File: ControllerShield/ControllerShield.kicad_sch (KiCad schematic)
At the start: 17 parts, among them J1 Power, J2 Digital/PWM, J3 Analog, J4 Digital/PWM, J5 Conn_02x05_Odd_Even, U1 COM-09032, U2 LIS3DH, U3 TLV75533PDBV

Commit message: Add switch to controller
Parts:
- added SW1: Small Switch TH, Footprints:SW4_1825910-B_TEC, symbol Local:Small Switch TH
- C1: Digikey (none) -> 1276-1000-1-ND
- C2: Digikey (none) -> 490-GRM188R61E106KA73JCT-ND
- D1: Digikey (none) -> 1125-1188-ND
- D2: Digikey (none) -> 1125-1184-ND
- R1, R2: Digikey (none) -> RMCF0603FT10K0CT-ND
- R3, R4: Digikey (none) -> RMCF0603FT1K00CT-ND
- U2: value LIS3DH -> LIS2DE12TR; Digikey (none) -> 497-15997-1-ND
- U3: Digikey (none) -> 296-50411-1-ND
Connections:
- net GND: now also SW1.3 (B), SW1.4 (B)
- net ~{RESET} renamed RSTn
- net RSTn: now also SW1.1 (A), SW1.2 (A)
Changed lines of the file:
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@@
+    (stroke (width 0) (type default))
+  )
+  (wire (pts (xy 54.61 138.43) (xy 63.5 138.43))
     (stroke (width 0) (type default))
   )
@@
     (effects (font (size 1.27 1.27)) (justify left bottom))
   )
-  (label "~{RESET}" (at 19.05 36.83 0) (fields_autoplaced)
-    (effects (font (size 1.27 1.27)) (justify left bottom))
+  (label "RSTn" (at 19.05 36.83 180) (fields_autoplaced)
+    (effects (font (size 1.27 1.27)) (justify right bottom))
   )
   (label "GameBtn" (at 68.58 72.39 0) (fields_autoplaced)
@@
   (label "X" (at 72.39 46.99 180) (fields_autoplaced)
     (effects (font (size 1.27 1.27)) (justify right bottom))
+  )
+  (label "RSTn" (at 55.88 138.43 0) (fields_autoplaced)
+    (effects (font (size 1.27 1.27)) (justify left bottom))
   )
   (label "D1" (at 69.85 39.37 0) (fields_autoplaced)
@@
     )
     (property "Datasheet" "~" (at 133.35 113.03 0)
+      (effects (font (size 1.27 1.27)) hide)
+    )
+    (property "Digikey" "RMCF0603FT10K0CT-ND" (at 133.35 113.03 0)
       (effects (font (size 1.27 1.27)) hide)
     )
@@
       (effects (font (size 1.27 1.27)) hide)
     )
+    (property "Digikey" "RMCF0603FT1K00CT-ND" (at 116.84 45.72 0)
+      (effects (font (size 1.27 1.27)) hide)
+    )
     (pin "1")
     (pin "2")
@@
         (path "/e63e39d7-6ac0-4ffd-8aa3-1841a4541b55"
           (reference "R4") (unit 1)
+        )
+      )
+    )
+  )
+  (symbol (lib_id "power:GND") (at 73.66 138.43 0) (unit 1)
+    (in_bom yes) (on_board yes) (dnp no) (fields_autoplaced)
+    (property "Reference" "#PWR011" (at 73.66 144.78 0)
+      (effects (font (size 1.27 1.27)) hide)
+    )
+    (property "Value" "GND" (at 73.66 143.51 0)
+      (effects (font (size 1.27 1.27)))
+    )
+    (property "Footprint" "" (at 73.66 138.43 0)
+      (effects (font (size 1.27 1.27)) hide)
+    )
+    (property "Datasheet" "" (at 73.66 138.43 0)
+      (effects (font (size 1.27 1.27)) hide)
+    )
+    (pin "1")
+    (instances
+      (project "ControllerShield"
+        (path "/e63e39d7-6ac0-4ffd-8aa3-1841a4541b55"
+          (reference "#PWR011") (unit 1)
         )
       )
@@
       (effects (font (size 1.27 1.27)) hide)
     )
-    (property "Datasheet" "~" (at 116.84 54.61 0)
+    (property "Datasheet" "https://marktechopto.com/pdf/products/datasheet/MT2118-G-A.pdf" (at 116.84 54.61 0)
+      (effects (font (size 1.27 1.27)) hide)
+    )
+    (property "Digikey" "1125-1184-ND" (at 116.84 54.61 0)
       (effects (font (size 1.27 1.27)) hide)
     )
@@
     )
     (property "Datasheet" "http://www.ti.com/lit/ds/symlink/tlv755p.pdf" (at 127 77.47 0)
+      (effects (font (size 1.27 1.27)) hide)
+    )
+    (property "Digikey" "296-50411-1-ND" (at 127 78.74 0)
       (effects (font (size 1.27 1.27)) hide)
     )
@@
       (effects (font (size 1.27 1.27)) hide)
     )
+    (property "Digikey" "RMCF0603FT10K0CT-ND" (at 130.81 113.03 0)
+      (effects (font (size 1.27 1.27)) hide)
+    )
     (pin "1")
     (pin "2")
@@
       (effects (font (size 1.27 1.27)) (justify left))
     )
-    (property "Value" "LIS3DH" (at 161.29 132.08 0)
+    (property "Value" "LIS2DE12TR" (at 161.29 132.08 0)
       (effects (font (size 1.27 1.27)) (justify left))
     )
@@
       (effects (font (size 1.27 1.27)) hide)
     )
-    (property "Datasheet" "https://www.st.com/resource/en/datasheet/cd00274221.pdf" (at 153.67 124.46 0)
+    (property "Datasheet" "https://www.st.com/content/ccc/resource/technical/document/datasheet/group0/72/cb/80/a7/5e/fe/46/9d/DM00153214/files/DM00153214.pdf/jcr:content/translations/en.DM00153214.pdf" (at 153.67 124.46 0)
+      (effects (font (size 1.27 1.27)) hide)
+    )
+    (property "Digikey" "497-15997-1-ND" (at 158.75 121.92 0)
       (effects (font (size 1.27 1.27)) hide)
     )
@@
       (effects (font (size 1.27 1.27)) hide)
     )
+    (property "Digikey" "1125-1188-ND" (at 109.22 54.61 0)
+      (effects (font (size 1.27 1.27)) hide)
+    )
     (pin "1")
     (pin "2")
@@
       (effects (font (size 1.27 1.27)) hide)
     )
+    (property "Digikey" "490-GRM188R61E106KA73JCT-ND" (at 191.77 118.11 0)
+      (effects (font (size 1.27 1.27)) hide)
+    )
     (pin "1")
     (pin "2")
@@
     )
   )
+  (symbol (lib_id "Local:Small Switch TH") (at 68.58 138.43 0) (unit 1)
+    (in_bom yes) (on_board yes) (dnp no) (fields_autoplaced)
+    (property "Reference" "SW1" (at 68.58 132.08 0)
+      (effects (font (size 1.27 1.27)))
+    )
+    (property "Value" "Small Switch TH" (at 68.58 134.62 0)
+      (effects (font (size 1.27 1.27)))
+    )
+    (property "Footprint" "Footprints:SW4_1825910-B_TEC" (at 68.58 138.43 0)
+      (effects (font (size 1.27 1.27)) hide)
+    )
+    (property "Datasheet" "https://www.te.com/usa-en/product-1825910-6.datasheet.pdf" (at 68.58 138.43 0)
+      (effects (font (size 1.27 1.27)) hide)
+    )
+    (property "Digikey" "450-1650-ND" (at 68.58 138.43 0)
+      (effects (font (size 1.27 1.27)) hide)
+    )
+    (pin "1")
+    (pin "2")
+    (pin "3")
+    (pin "4")
+    (instances
+      (project "ControllerShield"
+        (path "/e63e39d7-6ac0-4ffd-8aa3-1841a4541b55"
+          (reference "SW1") (unit 1)
+        )
+      )
+    )
+  )
   (symbol (lib_id "power:+3V3") (at 156.21 109.22 0) (unit 1)
     (in_bom yes) (on_board yes) (dnp no)
@@
       (effects (font (size 1.27 1.27)) hide)
     )
+    (property "Digikey" "1276-1000-1-ND" (at 180.34 118.11 0)
+      (effects (font (size 1.27 1.27)) hide)
+    )
     (pin "1")
     (pin "2")
@@
       (effects (font (size 1.27 1.27)) hide)
     )
+    (property "Digikey" "RMCF0603FT1K00CT-ND" (at 109.22 45.72 0)
+      (effects (font (size 1.27 1.27)) hide)
+    )

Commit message: add probe points
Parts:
- added J6: Debug Point, Connector_PinHeader_2.54mm:PinHeader_1x03_P2.54mm_Vertical, symbol Connector_Generic:Conn_01x03
- U2: value LIS2DE12TR -> LIS3DHTR; Digikey 497-15997-1-ND -> 497-10613-1-ND
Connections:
- net GND: now also J6.2 (Pin_2)
- net X: now also J6.1 (Pin_1)
- net Y: now also J6.3 (Pin_3)
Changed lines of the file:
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@@
     (date "2023-10-11")
   )
+  (junction (at 99.06 101.6) (diameter 0) (color 0 0 0 0)
+  )
   (junction (at 173.99 39.37) (diameter 0) (color 0 0 0 0)
+  )
+  (junction (at 81.28 101.6) (diameter 0) (color 0 0 0 0)
   )
   (junction (at 130.81 107.95) (diameter 0) (color 0 0 0 0)
@@
     (stroke (width 0) (type solid))
   )
+  (wire (pts (xy 88.9 91.44) (xy 88.9 93.98))
+    (stroke (width 0) (type default))
+  )
+  (wire (pts (xy 93.98 91.44) (xy 93.98 93.98))
+    (stroke (width 0) (type default))
+  )
   (wire (pts (xy 62.23 44.45) (xy 74.93 44.45))
     (stroke (width 0) (type solid))
@@
     (stroke (width 0) (type default))
   )
-  (wire (pts (xy 85.09 101.6) (xy 71.12 101.6))
+  (wire (pts (xy 85.09 101.6) (xy 81.28 101.6))
     (stroke (width 0) (type default))
   )
@@
     (stroke (width 0) (type default))
   )
+  (wire (pts (xy 93.98 93.98) (xy 99.06 93.98))
+    (stroke (width 0) (type default))
+  )
   (wire (pts (xy 177.8 72.39) (xy 177.8 77.47))
     (stroke (width 0) (type default))
@@
     (stroke (width 0) (type default))
   )
-  (wire (pts (xy 97.79 101.6) (xy 106.68 101.6))
+  (wire (pts (xy 97.79 101.6) (xy 99.06 101.6))
     (stroke (width 0) (type default))
   )
@@
     (stroke (width 0) (type solid))
   )
+  (wire (pts (xy 81.28 93.98) (xy 81.28 101.6))
+    (stroke (width 0) (type default))
+  )
   (wire (pts (xy 109.22 76.2) (xy 118.11 76.2))
     (stroke (width 0) (type default))
@@
     (stroke (width 0) (type solid))
   )
+  (wire (pts (xy 99.06 93.98) (xy 99.06 101.6))
+    (stroke (width 0) (type default))
+  )
   (wire (pts (xy 62.23 41.91) (xy 74.93 41.91))
     (stroke (width 0) (type solid))
   )
+  (wire (pts (xy 88.9 93.98) (xy 81.28 93.98))
+    (stroke (width 0) (type default))
+  )
   (wire (pts (xy 173.99 30.48) (xy 173.99 39.37))
     (stroke (width 0) (type default))
@@
     (stroke (width 0) (type default))
   )
+  (wire (pts (xy 81.28 101.6) (xy 71.12 101.6))
+    (stroke (width 0) (type default))
+  )
   (wire (pts (xy 21.59 67.31) (xy 34.29 67.31))
     (stroke (width 0) (type solid))
@@
   )
   (wire (pts (xy 133.35 115.57) (xy 133.35 124.46))
+    (stroke (width 0) (type default))
+  )
+  (wire (pts (xy 99.06 101.6) (xy 106.68 101.6))
     (stroke (width 0) (type default))
   )
@@
     )
   )
+  (symbol (lib_id "power:GND") (at 91.44 91.44 0) (unit 1)
+    (in_bom yes) (on_board yes) (dnp no) (fields_autoplaced)
+    (property "Reference" "#PWR025" (at 91.44 97.79 0)
+      (effects (font (size 1.27 1.27)) hide)
+    )
+    (property "Value" "GND" (at 91.44 96.52 0)
+      (effects (font (size 1.27 1.27)) hide)
+    )
+    (property "Footprint" "" (at 91.44 91.44 0)
+      (effects (font (size 1.27 1.27)) hide)
+    )
+    (property "Datasheet" "" (at 91.44 91.44 0)
+      (effects (font (size 1.27 1.27)) hide)
+    )
+    (pin "1")
+    (instances
+      (project "ControllerShield"
+        (path "/e63e39d7-6ac0-4ffd-8aa3-1841a4541b55"
+          (reference "#PWR025") (unit 1)
+        )
+      )
+    )
+  )
+  (symbol (lib_id "Connector_Generic:Conn_01x03") (at 91.44 86.36 90) (unit 1)
+    (in_bom yes) (on_board yes) (dnp no) (fields_autoplaced)
+    (property "Reference" "J6" (at 96.52 85.725 90)
+      (effects (font (size 1.27 1.27)) (justify right))
+    )
+    (property "Value" "Debug Point" (at 96.52 88.265 90)
+      (effects (font (size 1.27 1.27)) (justify right))
+    )
+    (property "Footprint" "Connector_PinHeader_2.54mm:PinHeader_1x03_P2.54mm_Vertical" (at 91.44 86.36 0)
+      (effects (font (size 1.27 1.27)) hide)
+    )
+    (property "Datasheet" "~" (at 91.44 86.36 0)
+      (effects (font (size 1.27 1.27)) hide)
+    )
+    (pin "1")
+    (pin "2")
+    (pin "3")
+    (instances
+      (project "ControllerShield"
+        (path "/e63e39d7-6ac0-4ffd-8aa3-1841a4541b55"
+          (reference "J6") (unit 1)
+        )
+      )
+    )
+  )
   (symbol (lib_id "Jumper:SolderJumper_2_Bridged") (at 124.46 132.08 90) (unit 1)
     (in_bom yes) (on_board yes) (dnp no) (fields_autoplaced)
@@
       (effects (font (size 1.27 1.27)) (justify left))
     )
-    (property "Value" "LIS2DE12TR" (at 161.29 132.08 0)
+    (property "Value" "LIS3DHTR" (at 161.29 132.08 0)
       (effects (font (size 1.27 1.27)) (justify left))
     )
@@
       (effects (font (size 1.27 1.27)) hide)
     )
-    (property "Digikey" "497-15997-1-ND" (at 158.75 121.92 0)
-      (effects (font (size 1.27 1.27)) hide)
-    )
+    (property "Digikey" "497-10613-1-ND" (at 158.75 121.92 0)
+      (effects (font (size 1.27 1.27)) hide)
+    )

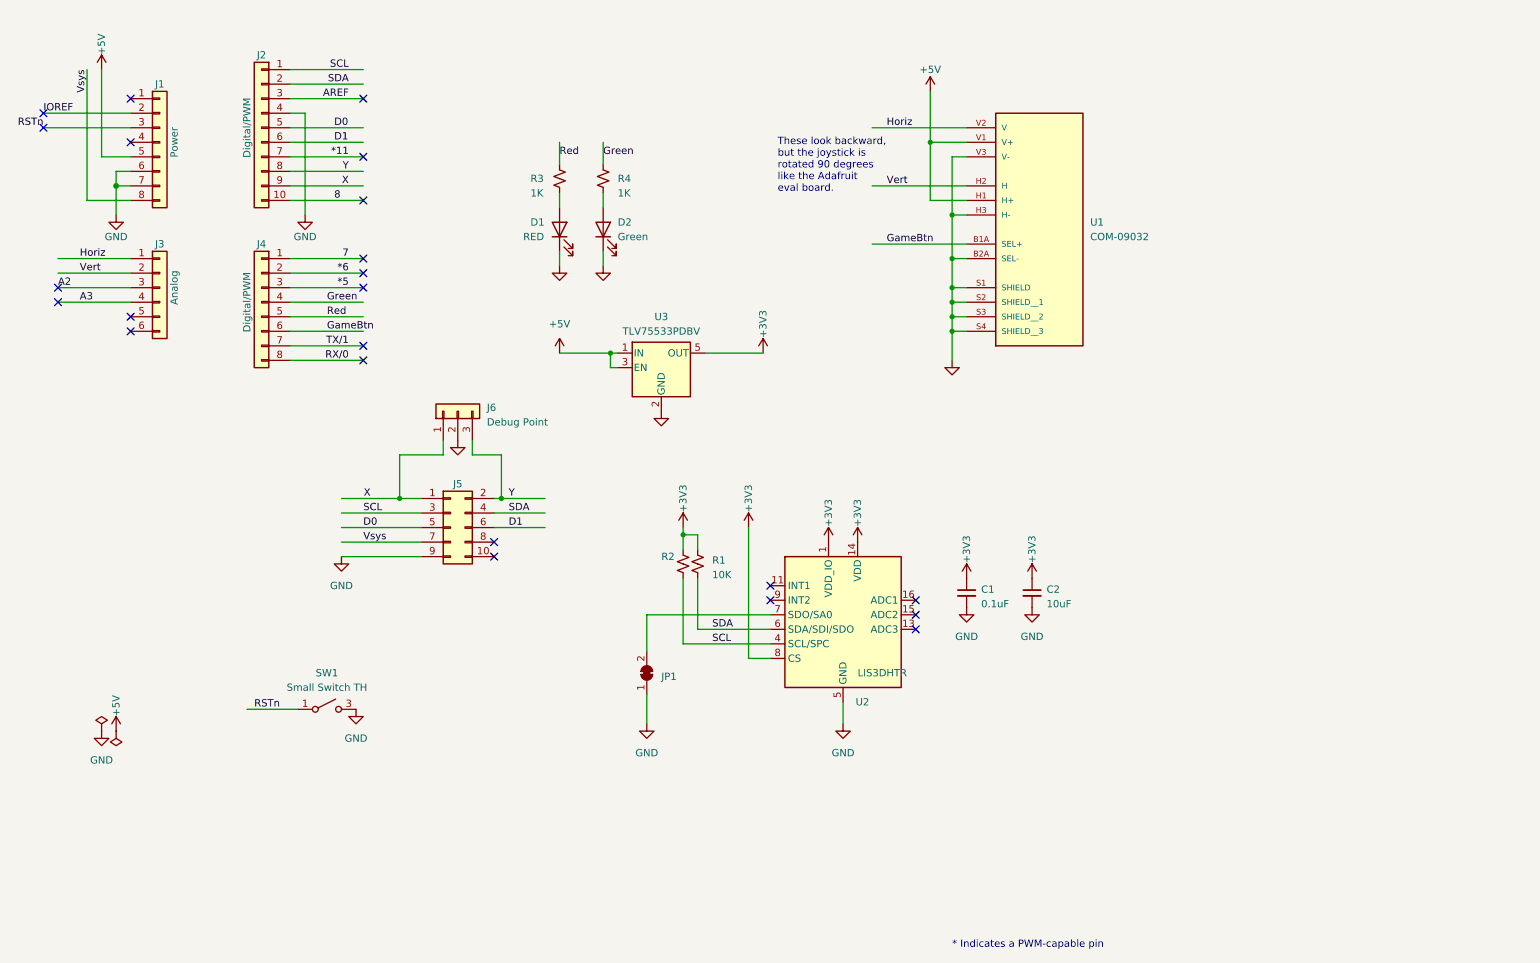
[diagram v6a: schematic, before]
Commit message: Add QR code in preparation for next release
Add Cap to

5V

Buttons

Add level shifter.

Close #7
Close #9
Close #11
Close #14
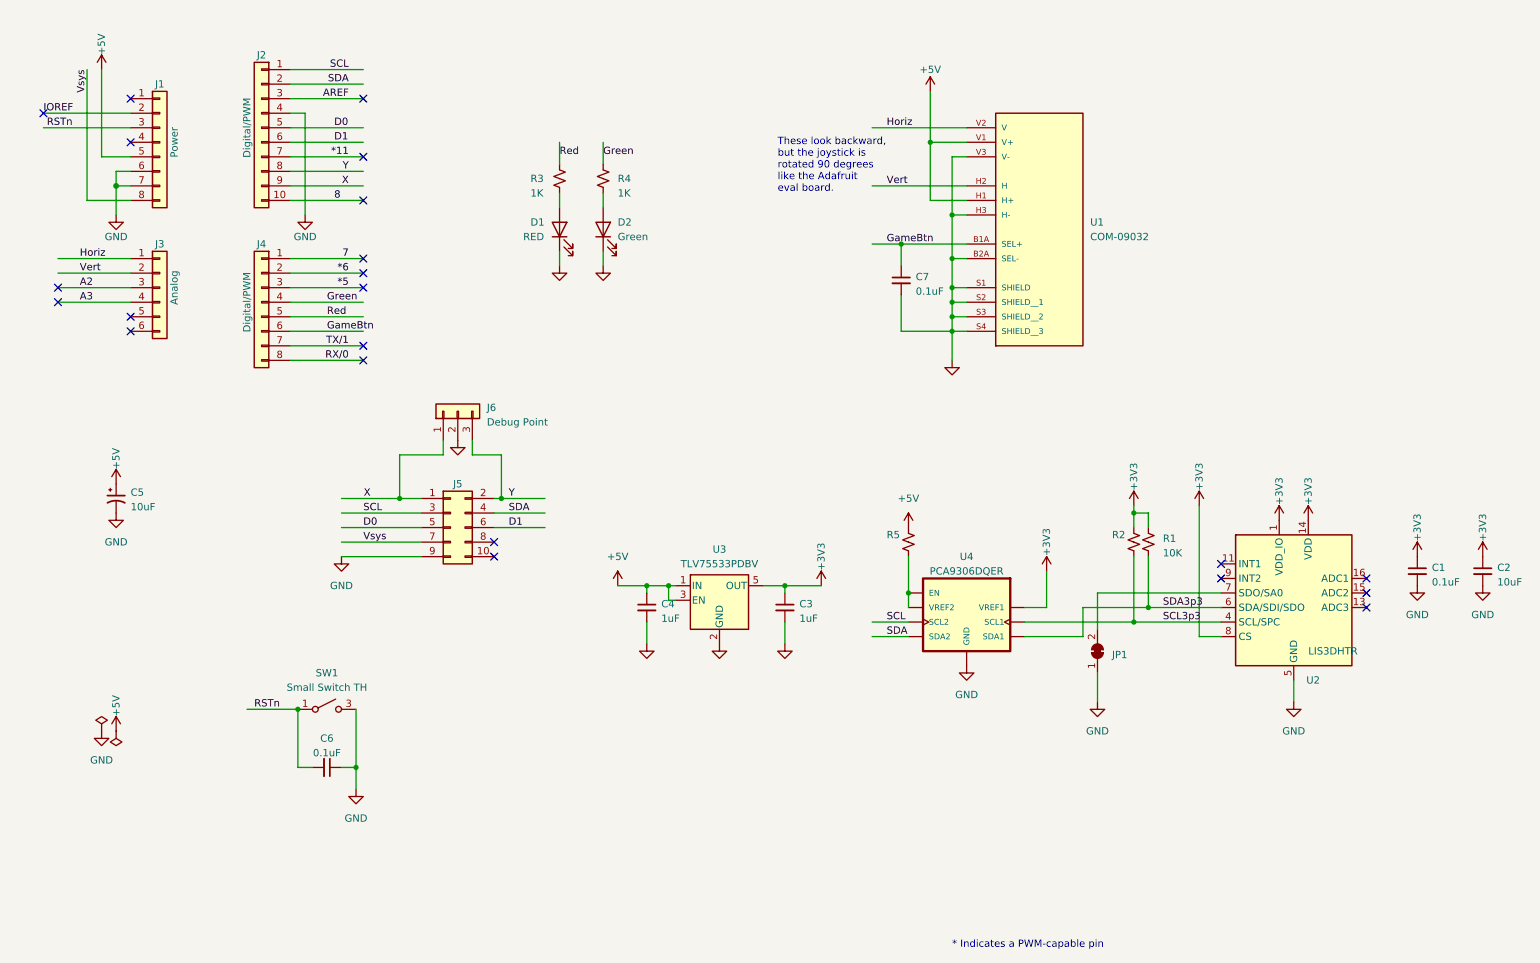
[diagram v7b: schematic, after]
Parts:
- added C3, C4: 1uF, Capacitor_SMD:C_0603_1608Metric, symbol Device:C_Small
- added C5: 10uF, Capacitor_THT:CP_Radial_D6.3mm_P2.50mm, symbol Device:C_Polarized_Small_US
- added C6, C7: 0.1uF, Capacitor_SMD:C_0603_1608Metric, symbol Device:C_Small
- added R5: 200K, Resistor_SMD:R_0603_1608Metric, symbol Device:R_Small_US
- added U4: PCA9306DQER, TexasInstruments:SON35P140X100X40-8N, symbol StockedComponents:PCA9306DQER
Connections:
- net +3V3: now also C3.1, U4.2 (VREF1)
- net +5V: now also C4.1, C5.1, R5.1
- net GND: now also C3.2, C4.2, C5.2, C6.1, C7.2, U4.1 (GND)
- net GameBtn: now also C7.1
- net RSTn: now also C6.2
- net SCL: now also U4.6 (SCL2); no longer R2.2, U2.4 (SCL/SPC)
- net SDA: now also U4.5 (SDA2); no longer R1.2, U2.6 (SDA/SDI/SDO)
- new net: R5.2, U4.7 (VREF2), U4.8 (EN)
- new net SCL3p3: R2.2, U2.4 (SCL/SPC), U4.3 (SCL1)
- new net SDA3p3: R1.2, U2.6 (SDA/SDI/SDO), U4.4 (SDA1)
- no-connect marks 23 -> 22
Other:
- moved on the sheet: C1, C2, JP1, R1, R2, U2, U3
